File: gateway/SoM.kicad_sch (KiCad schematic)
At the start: 11 parts, among them SW701 On / Off, SW702 Reset, X701 SoM

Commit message: Working on first version
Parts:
- removed SW701: On / Off, symbol Switch:SW_Push
- removed SW702: Reset, symbol Switch:SW_Push
- added R910, R911, R912: 10k, symbol Device:R
- added SW901: On / Off, Same Sky:TS11, symbol Switch:SW_Push_Shielded
- added SW903: Reset, Same Sky:TS11, symbol Switch:SW_Push_Shielded
- added TP903: ~, symbol Connector:TestPoint
- added X903: UART, Connector_PinHeader_2.54mm:PinHeader_1x03_P2.54mm_Vertical, symbol Connector_Generic:Conn_01x03
- C903: renamed from C701; footprint (none) -> Capacitor_SMD:C_0402_1005Metric; manf (none) -> KYOCERA AVX; manf# (none) -> 04025C104JAT2A
- JP901: renamed from JP701; footprint (none) -> Connector_PinHeader_2.54mm:PinHeader_2x01_P2.54mm_Vertical; now not fitted
- R906: renamed from R702; now in the parts list
- R907: renamed from R705; now in the parts list
- R908: renamed from R701; now in the parts list
- renumbered BT701 to BT901, R704 to R904, R703 to R905, X701 to X901
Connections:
- net GND: now also X901.229, SW901.2, SW901.SH (B), SW903.2, SW903.SH (B), X903.2 (Pin_2)
- net ~{CTRL_PWR_BTN_MICO}: now also SW901.1
- net ~{CTRL_RESET_MOCI}: now also TP903.1
- net at R904.1: now also SW903.1
- net I2C.SDA: now reaches X901.12
- net I2C.SCL: now reaches X901.14
- net LoRa-Power-Enable: now reaches X901.30
- net Zigbee-Power-Enable: now reaches X901.32
- net wm-Bus-Power-Enable: now reaches X901.34
- net ~{Battery-Charge-Enable}: now reaches X901.42
- net ~{Battery-Charge}: now reaches X901.44
- net ~{Battery-Alert}: now reaches X901.46
- net at X901.216: now also R910.2
- net at X901.218: now also R911.2
- net at X901.220: now also R912.2
- net PowerMux-Status: now reaches X901.222
- net Ethernet.TRD0_P: now reaches X901.225
- net Ethernet.TRD0_N: now reaches X901.227
- net Ethernet.TRD1_N: now reaches X901.231
- net Ethernet.TRD1_P: now reaches X901.233
- net Ethernet.LED-Yellow: now reaches X901.235
- net Ethernet.LED-Green: now reaches X901.237
- net Ethernet.TRD2_P: now reaches X901.239
- net Ethernet.TRD2_N: now reaches X901.241
- net Ethernet.TRD3_N: now reaches X901.245
- net Ethernet.TRD3_P: now reaches X901.247
- net Console-RxD: now reaches X901.129
- net Console-RxD: now also X903.1 (Pin_1)
- net Console-TxD: now reaches X901.131
- net Console-TxD: now also X903.3 (Pin_3)
- net USB.VBUS: now reaches X901.159
- net USB.ID: now reaches X901.161
- net USB.D_N: now reaches X901.163
- net USB.D_P: now reaches X901.165
- net USB-D_N renamed LoRa-USB.D_N
- net USB-D_P renamed LoRa-USB.D_P
- new net +1V8: R910.1, R911.1, R912.1
- no-connect marks 1 -> 28
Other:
- moved on the sheet: R905, R906, R907, R908

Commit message: Working on version 1.0
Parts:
- C903: footprint Capacitor_SMD:C_0402_1005Metric -> Capacitor_SMD:C_0805_2012Metric; manf# 04025C104JAT2A -> 08053C104M4T4A; mouser# (none) -> 581-08053C104M4T4A
- JP901: now left out of the parts list
- R905: renamed from R910; footprint (none) -> Resistor_SMD:R_0805_2012Metric; manf (none) -> Bourns; manf# (none) -> CR0805-FX-1002GLF; mouser# (none) -> 652-CR0805-FX-1002GLF
- R906: renamed from R911; footprint (none) -> Resistor_SMD:R_0805_2012Metric; manf (none) -> Bourns; manf# (none) -> CR0805-FX-1002GLF; mouser# (none) -> 652-CR0805-FX-1002GLF
- R907: renamed from R912; footprint (none) -> Resistor_SMD:R_0805_2012Metric; manf (none) -> Bourns; manf# (none) -> CR0805-FX-1002GLF; mouser# (none) -> 652-CR0805-FX-1002GLF
- R908: renamed from R905; footprint (none) -> Resistor_SMD:R_0805_2012Metric; manf (none) -> Bourns; manf# (none) -> CR0805-JW-103GLF; mouser# (none) -> 652-CR0805-JW-103GLF
- R909: renamed from R904; footprint (none) -> Resistor_SMD:R_0805_2012Metric; manf (none) -> Bourns; manf# (none) -> CR0805-FX-1001GLF; mouser# (none) -> 652-CR0805-FX-1001GLF
- R910: renamed from R907; footprint (none) -> Resistor_SMD:R_0805_2012Metric; now left out of the parts list
- R911: renamed from R906; footprint (none) -> Resistor_SMD:R_0805_2012Metric; now left out of the parts list
- R912: renamed from R908; footprint (none) -> Resistor_SMD:R_0805_2012Metric; now left out of the parts list
- TP904: renamed from TP903; footprint (none) -> Testpoints_Kampi:TestPoint_Pad_1.0x1.0mm
- renumbered SW903 to SW901, SW901 to SW902, X903 to X902

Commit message: Working on PCB
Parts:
- removed R911: ~, Resistor_SMD:R_0805_2012Metric, symbol Device:R
- added H903, H904: MountingHole, Wuerth:9774025151R, symbol Mechanical_Kampi:MountingHole
- X901: footprint TE:2309407-1 -> TE:2309409-2; manf# 2309407-1 -> 2309409-2; mouser# 571-2309407-1 -> 571-2309409-2
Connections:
- net +1V8: now also R908.1
- net Console-RxD: now also X901.147; no longer X901.129
- net Console-TxD: now also X901.149; no longer X901.131
- net GND: no longer X901.127
- net PWR_1V8_MOCI: no longer R908.1
- net GPIO.Num0: now reaches X901.17
- net GPIO.Num1: now reaches X901.19
- net GPIO.Num2: now reaches X901.21
- net GPIO.Num3: now reaches X901.53
- net GPIO.Num4: now reaches X901.55
- net GPIO.Num5: now reaches X901.91
- net GPIO.Num6: now reaches X901.93
- net GPIO.Num7: now reaches X901.95
- net PCIe.CLK_N: now reaches X901.226
- net PCIe.CLK_P: now reaches X901.228
- net PCIe.RX_P: now reaches X901.234
- net PCIe.RX_N: now reaches X901.236
- net PCIe.TX_N: now reaches X901.238
- net PCIe.TX_P: now reaches X901.240
- net PCIe.~{RST}: now reaches X901.244
- net wM-Bus.Reset: now reaches X901.102
- net Zigbee.Reset: now reaches X901.104
- net wM-Bus.RxD: now reaches X901.137
- net wM-Bus.TxD: now reaches X901.139
- net LoRa.Reset: now reaches X901.185
- net SSD-Power: now reaches X901.187
- net LoRa-USB.D_N renamed LoRa.D_N
- net LoRa-USB.D_P renamed LoRa.D_P
- net wm-Bus-Power-Enable renamed wM-Bus-Power-Enable
- new net Zigbee.RxD: X901.129
- new net Zigbee.TxD: X901.131
- no-connect marks 28 -> 169
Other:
- moved on the sheet: X901A, X902

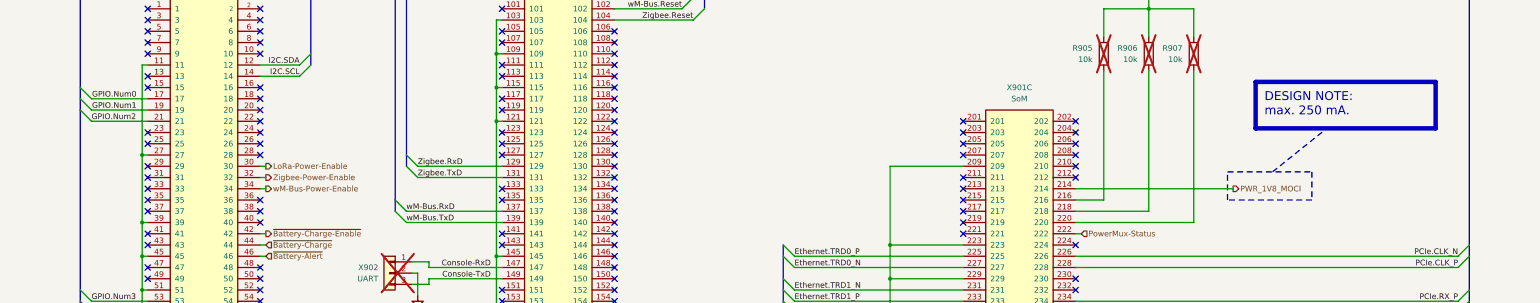
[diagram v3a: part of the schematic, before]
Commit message: Fix broken variant variable
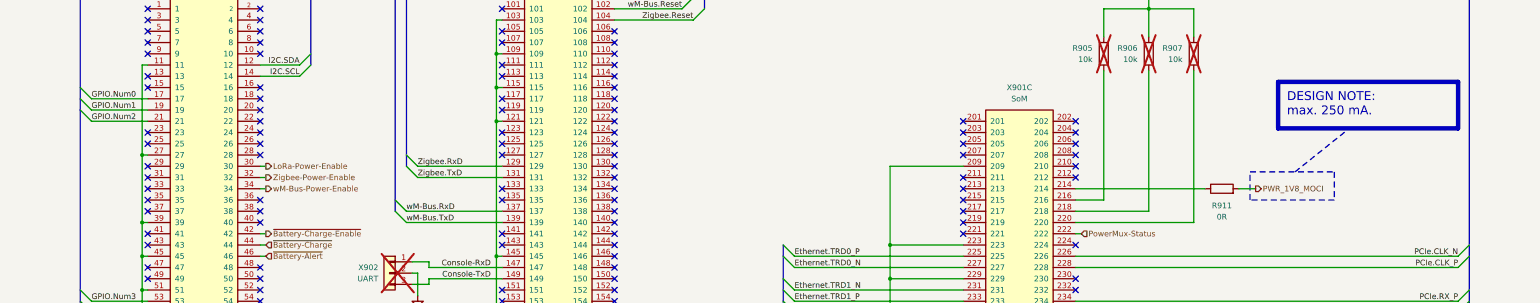
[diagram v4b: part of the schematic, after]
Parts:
- added R911: 0R, Resistor_SMD:R_0805_2012Metric, symbol Device:R
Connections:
- net PWR_1V8_MOCI: now also R911.2; no longer X901.214
- new net: R911.1, X901.214
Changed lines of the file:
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@@
 	)
 	(rectangle
-		(start 302.26 104.14)
-		(end 321.31 110.49)
+		(start 307.34 104.14)
+		(end 326.39 110.49)
 		(stroke
 			(width 0.254)
@@
 	(text_box "DESIGN NOTE:\nmax. 250 mA."
 		(exclude_from_sim no)
-		(at 308.61 83.82 0)
+		(at 313.69 83.82 0)
 		(size 40.64 10.494)
 		(margins 2 2 2 2)
@@
 	(wire
 		(pts
-			(xy 267.97 107.95) (xy 303.53 107.95)
+			(xy 267.97 107.95) (xy 297.18 107.95)
 		)
 		(stroke
@@
 	(polyline
 		(pts
-			(xy 312.42 104.14) (xy 325.12 93.98)
+			(xy 317.5 104.14) (xy 330.2 93.98)
 		)
 		(stroke
@@
 	(wire
 		(pts
+			(xy 304.8 107.95) (xy 308.61 107.95)
+		)
+		(stroke
+			(width 0)
+			(type default)
+		)
+	)
+	(wire
+		(pts
 			(xy 267.97 110.49) (xy 274.32 110.49)
 		)
@@
 	)
 	(label "GPIO.Num1"
-		(at 55.88 90.17 180)
+		(at 45.72 90.17 0)
 		(effects
 			(font
 				(size 1.27 1.27)
 			)
-			(justify right bottom)
+			(justify left bottom)
 		)
 	)
@@
 	)
 	(label "GPIO.Num0"
-		(at 55.88 87.63 180)
+		(at 45.72 87.63 0)
 		(effects
 			(font
 				(size 1.27 1.27)
 			)
-			(justify right bottom)
+			(justify left bottom)
 		)
 	)
@@
 	(hierarchical_label "PWR_1V8_MOCI"
 		(shape output)
-		(at 303.53 107.95 0)
+		(at 308.61 107.95 0)
 		(effects
 			(font
@@
 				)
 			)
+		)
+	)
+	(symbol
+		(lib_id "Device:R")
+		(at 300.99 107.95 90)
+		(unit 1)
+		(body_style 1)
+		(exclude_from_sim no)
+		(in_bom yes)
+		(on_board yes)
+		(in_pos_files yes)
+		(dnp no)
+		(fields_autoplaced yes)
+		(property "Reference" "R911"
+			(at 300.99 111.76 90)
+			(show_name no)
+			(do_not_autoplace no)
+			(effects
+				(font
+					(size 1.27 1.27)
+				)
+			)
+		)
+		(property "Value" "0R"
+			(at 300.99 114.3 90)
+			(show_name no)
+			(do_not_autoplace no)
+			(effects
+				(font
+					(size 1.27 1.27)
+				)
+			)
+		)
+		(property "Footprint" "Resistor_SMD:R_0805_2012Metric"
+			(at 300.99 109.728 90)
+			(hide yes)
+			(show_name no)
+			(do_not_autoplace no)
+			(effects
+				(font
+					(size 1.27 1.27)
+				)
+			)
+		)
+		(property "Datasheet" "https://www.mouser.de/datasheet/3/40/1/cr.pdf"
+			(at 300.99 107.95 0)
+			(hide yes)
+			(show_name no)
+			(do_not_autoplace no)
+			(effects
+				(font
+					(size 1.27 1.27)
+				)
+			)
+		)
+		(property "Description" "Resistor"
+			(at 300.99 107.95 0)
+			(hide yes)
+			(show_name no)
+			(do_not_autoplace no)
+			(effects
+				(font
+					(size 1.27 1.27)
+				)
+			)
+		)
+		(property "manf" "Bourns"
+			(at 300.99 107.95 0)
+			(hide yes)
+			(show_name no)
+			(do_not_autoplace no)
+			(effects
+				(font
+					(size 1.27 1.27)
+				)
+			)
+		)
+		(property "manf#" "CR0805-J/-000ELF"
+			(at 300.99 107.95 0)
+			(hide yes)
+			(show_name no)
+			(do_not_autoplace no)
+			(effects
+				(font
+					(size 1.27 1.27)
+				)
+			)
+		)
+		(property "mouser#" "652-CR0805-J/-000ELF"
+			(at 300.99 107.95 0)
+			(hide yes)
+			(show_name no)
+			(do_not_autoplace no)
+			(effects
+				(font
+					(size 1.27 1.27)
+				)
+			)
+		)
+		(pin "1"
+		)
+		(pin "2"
+		)
+		(instances
+			(project "Gateway"
+				(path "/d5742f03-3b1a-42e5-a384-018bd4b919aa/c5103ceb-5325-4a84-a025-9638a412984e/e744f3ce-03a6-44a6-8792-1447ef232b9a"
+					(reference "R911")
+					(unit 1)
+				)
+			)

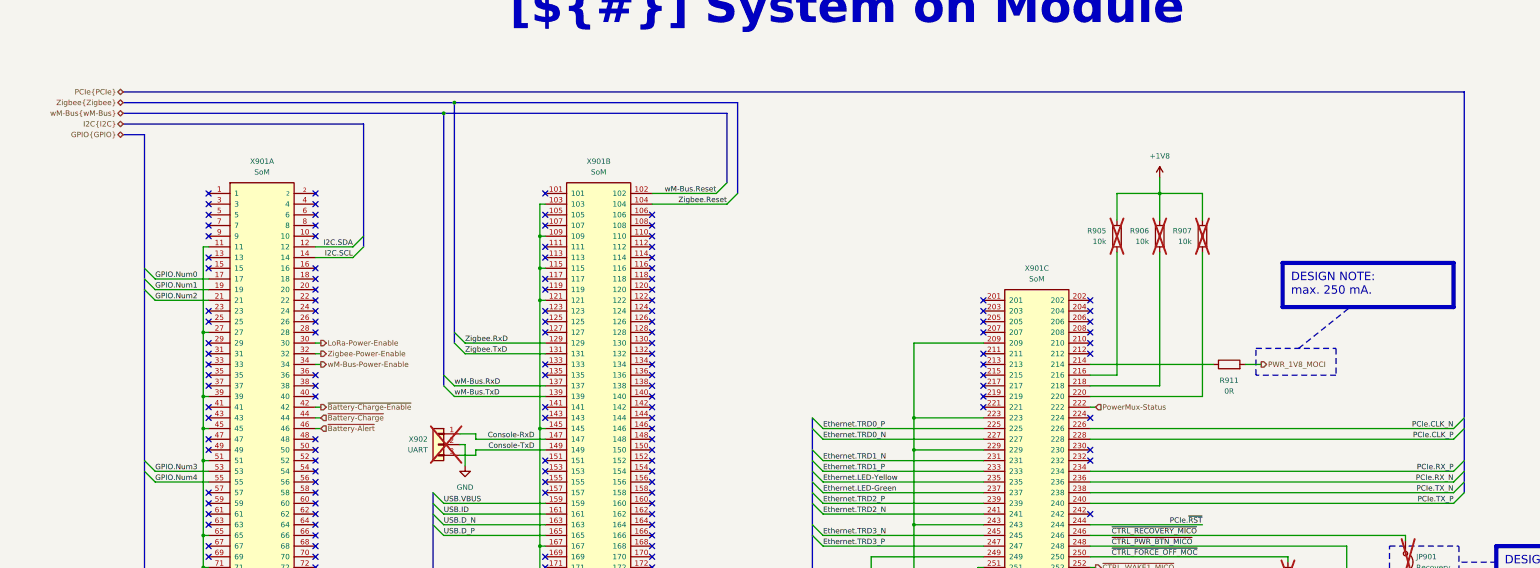
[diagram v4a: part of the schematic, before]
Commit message: Add WiFi antenna, add CAN interface
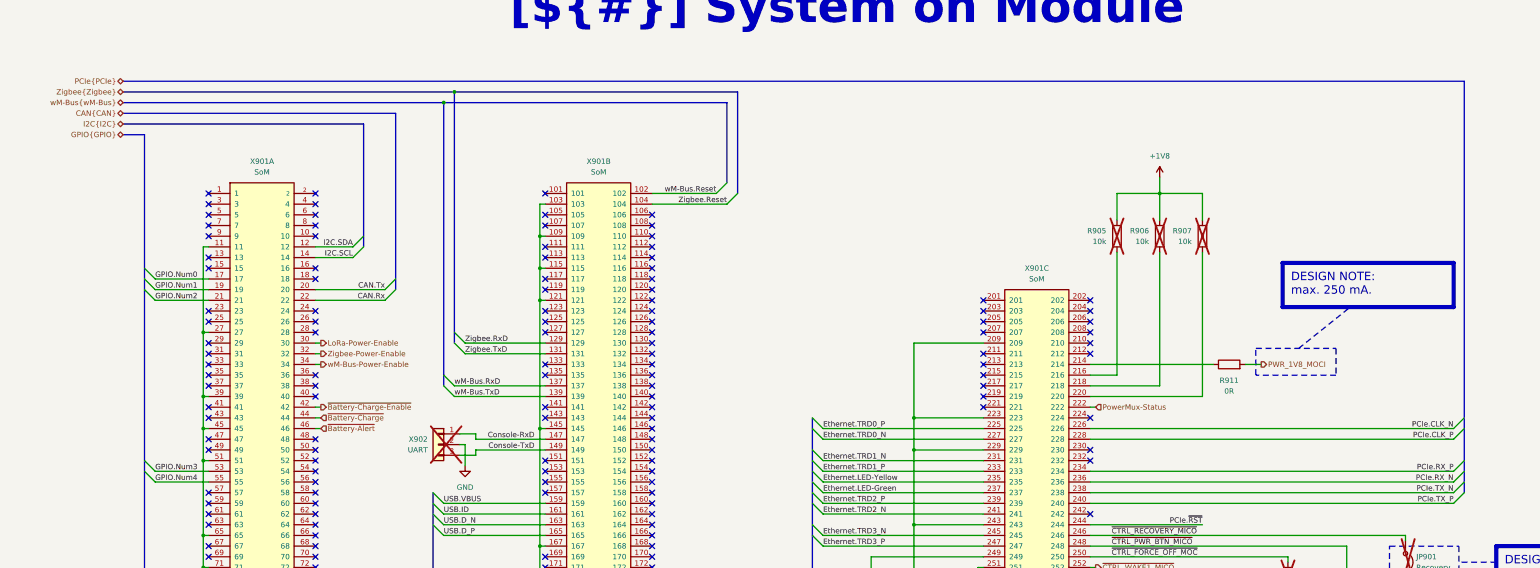
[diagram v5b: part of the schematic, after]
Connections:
- net CAN.Tx: now reaches X901.20
- net CAN.Rx: now reaches X901.22
- no-connect marks 169 -> 167
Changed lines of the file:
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@@
 	)
 	(junction
-		(at 116.84 45.72)
-		(diameter 0)
-		(color 0 0 0 0)
-	)
-	(junction
 		(at 137.16 186.69)
 		(diameter 0)
@@
 	)
 	(junction
-		(at 114.3 48.26)
-		(diameter 0)
-		(color 0 0 0 0)
-	)
-	(junction
 		(at 57.15 179.07)
 		(diameter 0)
@@
 	)
 	(junction
+		(at 114.3 45.72)
+		(diameter 0)
+		(color 0 0 0 0)
+	)
+	(junction
 		(at 137.16 123.19)
 		(diameter 0)
@@
 	)
 	(junction
+		(at 116.84 43.18)
+		(diameter 0)
+		(color 0 0 0 0)
+	)
+	(junction
 		(at 137.16 77.47)
 		(diameter 0)
@@
 	)
 	(no_connect
-		(at 83.82 90.17)
-	)
-	(no_connect
 		(at 138.43 133.35)
 	)
@@
 	)
 	(no_connect
-		(at 83.82 92.71)
-	)
-	(no_connect
 		(at 267.97 97.79)
 	)
@@
 	)
 	(bus_entry
+		(at 102.87 87.63)
+		(size -2.54 2.54)
+		(stroke
+			(width 0)
+			(type default)
+		)
+	)
+	(bus_entry
 		(at 114.3 168.91)
 		(size 2.54 2.54)
@@
 	)
 	(bus_entry
+		(at 102.87 90.17)
+		(size -2.54 2.54)
+		(stroke
+			(width 0)
+			(type default)
+		)
+	)
+	(bus_entry
 		(at 354.33 135.89)
 		(size 2.54 -2.54)
@@
 		)
 	)
-	(bus
-		(pts
-			(xy 114.3 48.26) (xy 114.3 110.49)
-		)
-		(stroke
-			(width 0)
-			(type default)
-		)
-	)
 	(wire
 		(pts
@@
 	(bus
 		(pts
-			(xy 184.15 67.31) (xy 184.15 45.72)
+			(xy 184.15 67.31) (xy 184.15 43.18)
 		)
 		(stroke
@@
 		)
 	)
+	(bus
+		(pts
+			(xy 116.84 43.18) (xy 116.84 102.87)
+		)
+		(stroke
+			(width 0)
+			(type default)
+		)
+	)
 	(wire
 		(pts
@@
 	(bus
 		(pts
-			(xy 116.84 102.87) (xy 116.84 45.72)
+			(xy 102.87 48.26) (xy 102.87 90.17)
 		)
 		(stroke
@@
 	(bus
 		(pts
-			(xy 114.3 48.26) (xy 181.61 48.26)
+			(xy 114.3 45.72) (xy 181.61 45.72)
 		)
 		(stroke
@@
 	(bus
 		(pts
-			(xy 181.61 48.26) (xy 181.61 64.77)
+			(xy 181.61 45.72) (xy 181.61 64.77)
+		)
+		(stroke
+			(width 0)
+			(type default)
+		)
+	)
+	(bus
+		(pts
+			(xy 38.1 48.26) (xy 102.87 48.26)
 		)
 		(stroke
@@
 	(bus
 		(pts
-			(xy 38.1 43.18) (xy 356.87 43.18)
+			(xy 38.1 40.64) (xy 356.87 40.64)
 		)
 		(stroke
@@
 	(bus
 		(pts
-			(xy 38.1 48.26) (xy 114.3 48.26)
+			(xy 38.1 45.72) (xy 114.3 45.72)
 		)
 		(stroke
@@
 	(wire
 		(pts
+			(xy 83.82 92.71) (xy 100.33 92.71)
+		)
+		(stroke
+			(width 0)
+			(type default)
+		)
+	)
+	(wire
+		(pts
 			(xy 267.97 118.11) (xy 269.24 118.11)
 		)
@@
 	(bus
 		(pts
-			(xy 116.84 45.72) (xy 184.15 45.72)
+			(xy 116.84 43.18) (xy 184.15 43.18)
+		)
+		(stroke
+			(width 0)
+			(type default)
+		)
+	)
+	(bus
+		(pts
+			(xy 114.3 45.72) (xy 114.3 110.49)
 		)
 		(stroke
@@
 	(bus
 		(pts
-			(xy 356.87 43.18) (xy 356.87 138.43)
+			(xy 356.87 40.64) (xy 356.87 138.43)
 		)
 		(stroke
@@
 	(bus
 		(pts
-			(xy 38.1 45.72) (xy 116.84 45.72)
+			(xy 38.1 43.18) (xy 116.84 43.18)
 		)
 		(stroke
@@
 	(wire
 		(pts
+			(xy 100.33 90.17) (xy 83.82 90.17)
+		)
+		(stroke
+			(width 0)
+			(type default)
+		)
+	)
+	(wire
+		(pts
 			(xy 242.57 163.83) (xy 241.3 163.83)
 		)
@@
 		)
 	)
+	(label "CAN.Tx"
+		(at 100.33 90.17 180)
+		(effects
+			(font
+				(size 1.27 1.27)
+			)
+			(justify right bottom)
+		)
+	)
 	(label "~{CTRL_RECOVERY_MICO}"
 		(at 273.05 148.59 0)
@@
 		)
 	)
+	(label "CAN.Rx"
+		(at 100.33 92.71 180)
+		(effects
+			(font
+				(size 1.27 1.27)
+			)
+			(justify right bottom)
+		)
+	)
 	(label "Ethernet.TRD2_P"
 		(at 204.47 140.97 0)
@@
 	(hierarchical_label "PCIe{PCIe}"
 		(shape bidirectional)
-		(at 38.1 43.18 180)
+		(at 38.1 40.64 180)
 		(effects
 			(font
@@
 		)
 	)
-	(hierarchical_label "wM-Bus{wM-Bus}"
+	(hierarchical_label "CAN{CAN}"
 		(shape bidirectional)
 		(at 38.1 48.26 180)
@@
 		)
 	)
+	(hierarchical_label "wM-Bus{wM-Bus}"
+		(shape bidirectional)
+		(at 38.1 45.72 180)
+		(effects
+			(font
+				(size 1.27 1.27)
+			)
+			(justify right)
+		)
+	)
 	(hierarchical_label "SoM-Power-Enable"
 		(shape output)
@@
 	(hierarchical_label "Zigbee{Zigbee}"
 		(shape bidirectional)
-		(at 38.1 45.72 180)
+		(at 38.1 43.18 180)
 		(effects
 			(font

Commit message: Working on version 1.0.0
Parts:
- H903, H904: footprint Wuerth:9774025151R -> Wuerth:9774015151R; manf# 9774025151R -> 9774015151R; mouser# 710-9774025151R -> 710-9774015151R
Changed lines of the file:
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@@
 			)
 		)
-		(property "Footprint" "Wuerth:9774025151R"
+		(property "Footprint" "Wuerth:9774015151R"
 			(at 201.93 279.4 0)
 			(hide yes)
@@
 			)
 		)
-		(property "Datasheet" "https://www.we-online.com/components/products/datasheet/9774025151R.pdf"
+		(property "Datasheet" "https://www.we-online.com/components/products/datasheet/9774015151R.pdf"
 			(at 201.93 279.4 0)
 			(hide yes)
@@
 			)
 		)
-		(property "manf#" "9774025151R"
+		(property "manf#" "9774015151R"
 			(at 201.93 279.4 0)
 			(hide yes)
@@
 			)
 		)
-		(property "mouser#" "710-9774025151R"
+		(property "mouser#" "710-9774015151R"
 			(at 201.93 279.4 0)
 			(hide yes)
@@
 			)
 		)
+		(property "Sim.Device" "V"
+			(at 215.9 168.91 0)
+			(hide yes)
+			(show_name no)
+			(do_not_autoplace no)
+			(effects
+				(font
+					(size 1.27 1.27)
+				)
+			)
+		)
+		(property "Sim.Type" "DC"
+			(at 215.9 168.91 0)
+			(hide yes)
+			(show_name no)
+			(do_not_autoplace no)
+			(effects
+				(font
+					(size 1.27 1.27)
+				)
+			)
+		)
+		(property "Sim.Pins" "1=+ 2=-"
+			(at 215.9 168.91 0)
+			(hide yes)
+			(show_name no)
+			(do_not_autoplace no)
+			(effects
+				(font
+					(size 1.27 1.27)
+				)
+			)
+		)
 		(pin "1"
 		)
@@
 			)
 		)
-		(property "Footprint" "Wuerth:9774025151R"
+		(property "Footprint" "Wuerth:9774015151R"
 			(at 195.58 279.4 0)
 			(hide yes)
@@
 			)
 		)
-		(property "Datasheet" "https://www.we-online.com/components/products/datasheet/9774025151R.pdf"
+		(property "Datasheet" "https://www.we-online.com/components/products/datasheet/9774015151R.pdf"
 			(at 195.58 279.4 0)
 			(hide yes)
@@
 			)
 		)
-		(property "manf#" "9774025151R"
+		(property "manf#" "9774015151R"
 			(at 195.58 279.4 0)
 			(hide yes)
@@
 			)
 		)
-		(property "mouser#" "710-9774025151R"
+		(property "mouser#" "710-9774015151R"
 			(at 195.58 279.4 0)
 			(hide yes)

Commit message: Working on version 1.0.0
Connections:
- net GPIO.Num3: now also X901.94; no longer X901.53
- net GPIO.Num4: now also X901.96; no longer X901.55
- net PCIe.~{CLK-REQ}: now also X901.151
- net Thread-Power-Enable: now reaches X901.36
- net Thread.RTS: now reaches X901.202
- net Thread.Reset: now reaches X901.106
- net Zigbee.CTS: now reaches X901.133
- net Zigbee.RTS: now reaches X901.135
- net wM-Bus.CTS: now reaches X901.141
- net wM-Bus.RTS: now reaches X901.143
- net Thread.RxD: now reaches X901.196
- net Thread.CTS: now reaches X901.198
- net Thread.TxD: now reaches X901.200
- no-connect marks 167 -> 156
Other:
- moved on the sheet: R905, R906, R907, R911, X901B, X902

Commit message: Working on version 1.0.0
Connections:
- net SSD-Power renamed SSD-Power-Enable
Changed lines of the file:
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@@
 		)
 	)
-	(hierarchical_label "SSD-Power"
+	(hierarchical_label "SSD-Power-Enable"
 		(shape output)
 		(at 140.97 176.53 180)
